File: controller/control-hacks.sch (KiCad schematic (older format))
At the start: 27 parts, among them K18 RELAY_SEPARATED, K19 RELAY_SEPARATED, K20 RELAY_SEPARATED, K21 RELAY_SEPARATED, K22 RELAY_SEPARATED, K23 RELAY_SEPARATED, K24 RELAY_SEPARATED, K25 RELAY_SEPARATED, K26 RELAY_SEPARATED

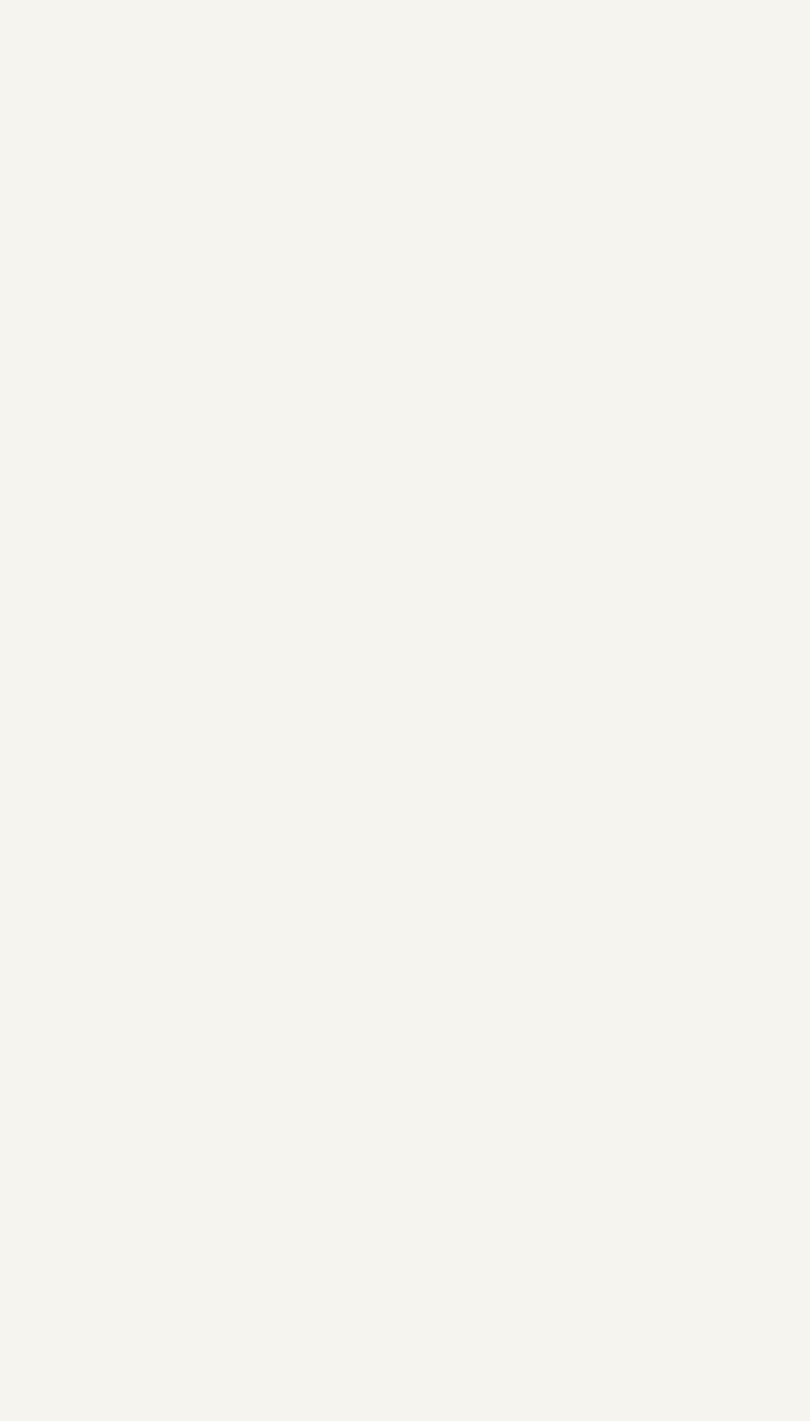
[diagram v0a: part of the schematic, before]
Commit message: Change gas pedal interface so that it supports going up and down from the middle voltage so that it's compatible with Linde forklift gas mechanism
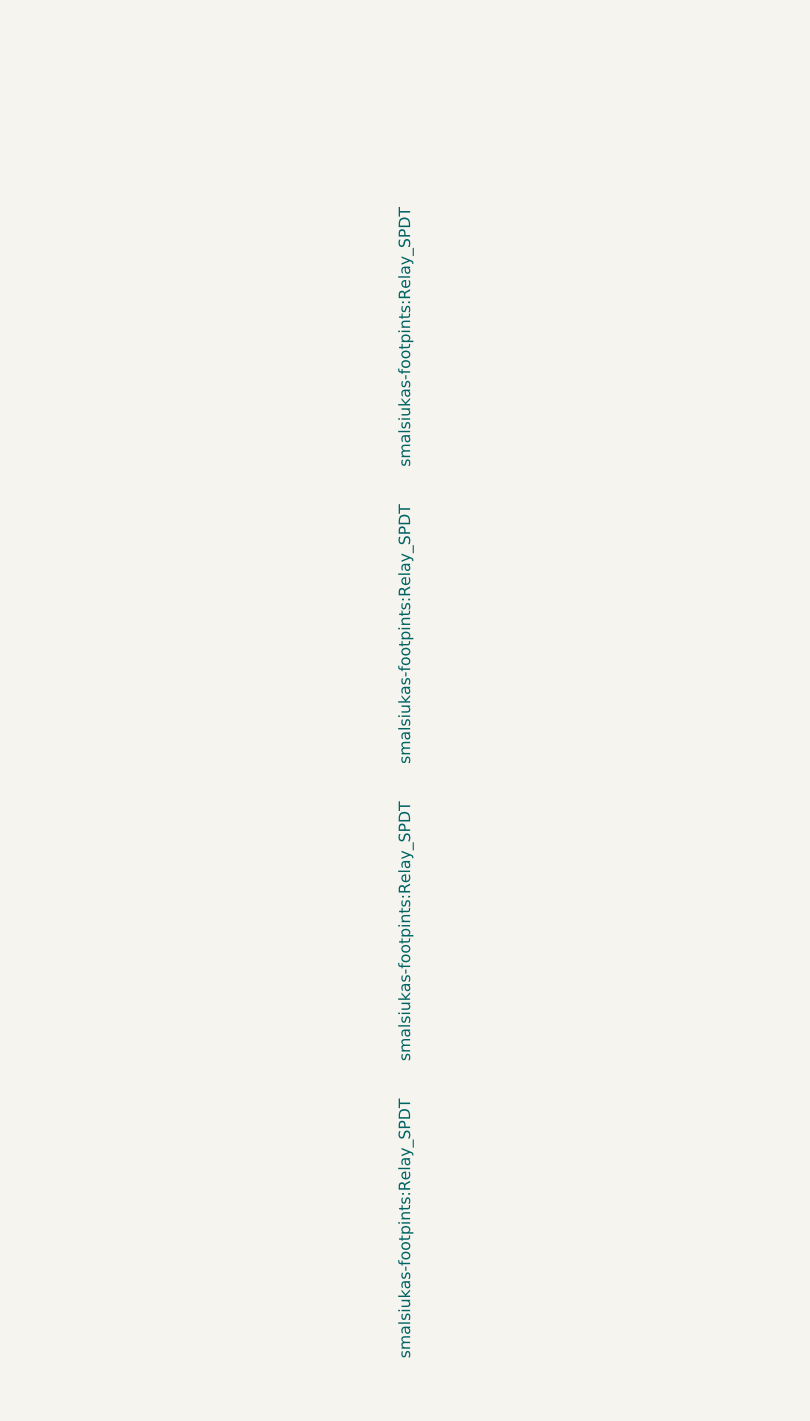
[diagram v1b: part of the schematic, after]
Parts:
- C23, C24, C25, C26, C27, C28, C29, C30, C31: footprint (none) -> Capacitors_SMD:C_0603_HandSoldering
- D18, D19, D20, D21, D22, D23, D24, D25, D26: footprint (none) -> Diodes_SMD:D_SOD-123
- K18, K19, K20, K21: footprint (none) -> smalsiukas-footpints:Relay_SPDT; Distributor (none) -> ?; Manufacturer (none) -> ?; PartNo (none) -> ?
- K18, K19, K20, K21, K22, K23, K24, K25, K26: footprint (none) -> smalsiukas-footpints:Relay_SPDT
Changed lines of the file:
@@
 F 0 "K24" V 7016 4700 50  0000 C CNN
 F 1 "RELAY_SEPARATED" V 7016 4700 50  0001 C CNN
-F 2 "" H 2150 100 50  0000 C CNN
+F 2 "smalsiukas-footpints:Relay_SPDT" H 2150 100 50  0001 C CNN
 F 3 "" H 2150 100 50  0000 C CNN
 F 4 "?" H 7250 4700 60  0001 C CNN "PartNo"
@@
 F 0 "K22" V 3100 1150 50  0000 C CNN
 F 1 "RELAY_SEPARATED" V 3066 1150 50  0001 C CNN
-F 2 "" H -1800 -3450 50  0000 C CNN
+F 2 "smalsiukas-footpints:Relay_SPDT" H -1800 -3450 50  0001 C CNN
 F 3 "" H -1800 -3450 50  0000 C CNN
 F 4 "?" H 3300 1150 60  0001 C CNN "PartNo"
@@
 F 0 "K22" V 7016 3700 50  0000 C CNN
 F 1 "RELAY_SEPARATED" V 7016 3700 50  0001 C CNN
-F 2 "" H 2150 -900 50  0000 C CNN
+F 2 "smalsiukas-footpints:Relay_SPDT" H 2150 -900 50  0001 C CNN
 F 3 "" H 2150 -900 50  0000 C CNN
 F 4 "?" H 7250 3700 60  0001 C CNN "PartNo"
@@
 F 0 "K23" V 3066 2450 50  0000 C CNN
 F 1 "RELAY_SEPARATED" V 3066 2450 50  0001 C CNN
-F 2 "" H -1800 -2150 50  0000 C CNN
+F 2 "smalsiukas-footpints:Relay_SPDT" H -1800 -2150 50  0001 C CNN
 F 3 "" H -1800 -2150 50  0000 C CNN
 F 4 "?" H 3300 2450 60  0001 C CNN "PartNo"
@@
 F 0 "K23" V 7016 4250 50  0000 C CNN
 F 1 "RELAY_SEPARATED" V 7016 4250 50  0001 C CNN
-F 2 "" H 2150 -350 50  0000 C CNN
+F 2 "smalsiukas-footpints:Relay_SPDT" H 2150 -350 50  0001 C CNN
 F 3 "" H 2150 -350 50  0000 C CNN
 F 4 "?" H 7250 4250 60  0001 C CNN "PartNo"
@@
 F 0 "K24" V 3066 3750 50  0000 C CNN
 F 1 "RELAY_SEPARATED" V 3066 3750 50  0001 C CNN
-F 2 "" H -1800 -850 50  0000 C CNN
+F 2 "smalsiukas-footpints:Relay_SPDT" H -1800 -850 50  0001 C CNN
 F 3 "" H -1800 -850 50  0000 C CNN
 F 4 "?" H 3300 3750 60  0001 C CNN "PartNo"
@@
 F 0 "K25" V 3066 5050 50  0000 C CNN
 F 1 "RELAY_SEPARATED" V 3066 5050 50  0001 C CNN
-F 2 "" H -1800 450 50  0000 C CNN
+F 2 "smalsiukas-footpints:Relay_SPDT" H -1800 450 50  0001 C CNN
 F 3 "" H -1800 450 50  0000 C CNN
 F 4 "?" H 3300 5050 60  0001 C CNN "PartNo"
@@
 F 0 "K25" V 7016 5150 50  0000 C CNN
 F 1 "RELAY_SEPARATED" V 7016 5150 50  0001 C CNN
-F 2 "" H 2150 550 50  0000 C CNN
+F 2 "smalsiukas-footpints:Relay_SPDT" H 2150 550 50  0001 C CNN
 F 3 "" H 2150 550 50  0000 C CNN
 F 4 "?" H 7250 5150 60  0001 C CNN "PartNo"
@@
 F 0 "K26" V 3066 6300 50  0000 C CNN
 F 1 "RELAY_SEPARATED" V 3066 6300 50  0001 C CNN
-F 2 "" H -1800 1700 50  0000 C CNN
+F 2 "smalsiukas-footpints:Relay_SPDT" H -1800 1700 50  0001 C CNN
 F 3 "" H -1800 1700 50  0000 C CNN
 F 4 "?" H 3300 6300 60  0001 C CNN "PartNo"
@@
 F 0 "D18" V 954 1571 50  0000 R CNN
 F 1 "D_ALT" V 1045 1571 50  0000 R CNN
-F 2 "" H -3900 -650 50  0001 C CNN
+F 2 "Diodes_SMD:D_SOD-123" H -3900 -650 50  0001 C CNN
 F 3 "" H -3900 -650 50  0001 C CNN
 	1    1000 1650
@@
 F 0 "C23" H 1115 1996 50  0000 L CNN
 F 1 "C" H 1115 1905 50  0000 L CNN
-F 2 "" H -962 0   50  0001 C CNN
+F 2 "Capacitors_SMD:C_0603_HandSoldering" H -962 0   50  0001 C CNN
 F 3 "" H -1000 150 50  0001 C CNN
 	1    1000 1950
@@
 F 0 "K18" H 1205 1196 50  0000 L CNN
 F 1 "RELAY_SEPARATED" H 1205 1105 50  0001 L CNN
-F 2 "" H -6600 -3150 50  0000 C CNN
+F 2 "smalsiukas-footpints:Relay_SPDT" H -6600 -3150 50  0000 C CNN
 F 3 "" H -6600 -3150 50  0000 C CNN
+F 4 "?" H 1050 1150 60  0001 C CNN "PartNo"
+F 5 "?" H 1050 1150 60  0001 C CNN "Manufacturer"
+F 6 "?" H 1050 1150 60  0001 C CNN "Distributor"
 	1    1050 1150
 	0    -1   -1   0
@@
 F 0 "D19" V 954 2871 50  0000 R CNN
 F 1 "D_ALT" V 1045 2871 50  0000 R CNN
-F 2 "" H -3900 650 50  0001 C CNN
+F 2 "Diodes_SMD:D_SOD-123" H -3900 650 50  0001 C CNN
 F 3 "" H -3900 650 50  0001 C CNN
 	1    1000 2950
@@
 F 0 "C24" H 1115 3296 50  0000 L CNN
 F 1 "C" H 1115 3205 50  0000 L CNN
-F 2 "" H -962 1300 50  0001 C CNN
+F 2 "Capacitors_SMD:C_0603_HandSoldering" H -962 1300 50  0001 C CNN
 F 3 "" H -1000 1450 50  0001 C CNN
 	1    1000 3250
@@
 F 0 "K18" V 7016 1550 50  0000 C CNN
 F 1 "RELAY_SEPARATED" H 7405 1505 50  0001 L CNN
-F 2 "" H -400 -2750 50  0000 C CNN
+F 2 "smalsiukas-footpints:Relay_SPDT" H -400 -2750 50  0001 C CNN
 F 3 "" H -400 -2750 50  0000 C CNN
 	2    7250 1550
@@
 F 0 "D20" V 954 4171 50  0000 R CNN
 F 1 "D_ALT" V 1045 4171 50  0000 R CNN
-F 2 "" H -3900 1950 50  0001 C CNN
+F 2 "Diodes_SMD:D_SOD-123" H -3900 1950 50  0001 C CNN
 F 3 "" H -3900 1950 50  0001 C CNN
 	1    1000 4250
@@
 F 0 "C25" H 1115 4596 50  0000 L CNN
 F 1 "C" H 1115 4505 50  0000 L CNN
-F 2 "" H -962 2600 50  0001 C CNN
+F 2 "Capacitors_SMD:C_0603_HandSoldering" H -962 2600 50  0001 C CNN
 F 3 "" H -1000 2750 50  0001 C CNN
 	1    1000 4550
@@
 F 0 "K19" H 1205 2496 50  0000 L CNN
 F 1 "RELAY_SEPARATED" H 1205 2405 50  0001 L CNN
-F 2 "" H -6600 -1850 50  0000 C CNN
+F 2 "smalsiukas-footpints:Relay_SPDT" H -6600 -1850 50  0000 C CNN
 F 3 "" H -6600 -1850 50  0000 C CNN
+F 4 "?" H 1050 2450 60  0001 C CNN "PartNo"
+F 5 "?" H 1050 2450 60  0001 C CNN "Manufacturer"
+F 6 "?" H 1050 2450 60  0001 C CNN "Distributor"
 	1    1050 2450
 	0    -1   -1   0
@@
 F 0 "D21" V 954 5471 50  0000 R CNN
 F 1 "D_ALT" V 1045 5471 50  0000 R CNN
-F 2 "" H -3900 3250 50  0001 C CNN
+F 2 "Diodes_SMD:D_SOD-123" H -3900 3250 50  0001 C CNN
 F 3 "" H -3900 3250 50  0001 C CNN
 	1    1000 5550
@@
 F 0 "C26" H 1115 5896 50  0000 L CNN
 F 1 "C" H 1115 5805 50  0000 L CNN
-F 2 "" H -962 3900 50  0001 C CNN
+F 2 "Capacitors_SMD:C_0603_HandSoldering" H -962 3900 50  0001 C CNN
 F 3 "" H -1000 4050 50  0001 C CNN
 	1    1000 5850
@@
 F 0 "K19" V 7016 2100 50  0000 C CNN
 F 1 "RELAY_SEPARATED" H 7405 2055 50  0001 L CNN
-F 2 "" H -400 -2200 50  0000 C CNN
+F 2 "smalsiukas-footpints:Relay_SPDT" H -400 -2200 50  0001 C CNN
 F 3 "" H -400 -2200 50  0000 C CNN
 	2    7250 2100
@@
 F 0 "D22" V 3204 1571 50  0000 R CNN
 F 1 "D_ALT" V 3295 1571 50  0000 R CNN
-F 2 "" H -1650 -650 50  0001 C CNN
+F 2 "Diodes_SMD:D_SOD-123" H -1650 -650 50  0001 C CNN
 F 3 "" H -1650 -650 50  0001 C CNN
 	1    3250 1650
@@
 F 0 "C27" H 3365 1996 50  0000 L CNN
 F 1 "C" H 3365 1905 50  0000 L CNN
-F 2 "" H 1288 0   50  0001 C CNN
+F 2 "Capacitors_SMD:C_0603_HandSoldering" H 1288 0   50  0001 C CNN
 F 3 "" H 1250 150 50  0001 C CNN
 	1    3250 1950
@@
 F 0 "K20" H 1205 3796 50  0000 L CNN
 F 1 "RELAY_SEPARATED" H 1205 3705 50  0001 L CNN
-F 2 "" H -6600 -550 50  0000 C CNN
+F 2 "smalsiukas-footpints:Relay_SPDT" H -6600 -550 50  0000 C CNN
 F 3 "" H -6600 -550 50  0000 C CNN
+F 4 "?" H 1050 3750 60  0001 C CNN "PartNo"
+F 5 "?" H 1050 3750 60  0001 C CNN "Manufacturer"
+F 6 "?" H 1050 3750 60  0001 C CNN "Distributor"
 	1    1050 3750
 	0    -1   -1   0
@@
 F 0 "D23" V 3204 2871 50  0000 R CNN
 F 1 "D_ALT" V 3295 2871 50  0000 R CNN
-F 2 "" H -1650 650 50  0001 C CNN
+F 2 "Diodes_SMD:D_SOD-123" H -1650 650 50  0001 C CNN
 F 3 "" H -1650 650 50  0001 C CNN
 	1    3250 2950
@@
 F 0 "C28" H 3365 3296 50  0000 L CNN
 F 1 "C" H 3365 3205 50  0000 L CNN
-F 2 "" H 1288 1300 50  0001 C CNN
+F 2 "Capacitors_SMD:C_0603_HandSoldering" H 1288 1300 50  0001 C CNN
 F 3 "" H 1250 1450 50  0001 C CNN
 	1    3250 3250
@@
 F 0 "K20" V 7016 2650 50  0000 C CNN
 F 1 "RELAY_SEPARATED" H 7405 2605 50  0001 L CNN
-F 2 "" H -400 -1650 50  0000 C CNN
+F 2 "smalsiukas-footpints:Relay_SPDT" H -400 -1650 50  0001 C CNN
 F 3 "" H -400 -1650 50  0000 C CNN
 	2    7250 2650
@@
 F 0 "D24" V 3204 4171 50  0000 R CNN
 F 1 "D_ALT" V 3295 4171 50  0000 R CNN
-F 2 "" H -1650 1950 50  0001 C CNN
+F 2 "Diodes_SMD:D_SOD-123" H -1650 1950 50  0001 C CNN
 F 3 "" H -1650 1950 50  0001 C CNN
 	1    3250 4250
@@
 F 0 "C29" H 3365 4596 50  0000 L CNN
 F 1 "C" H 3365 4505 50  0000 L CNN
-F 2 "" H 1288 2600 50  0001 C CNN
+F 2 "Capacitors_SMD:C_0603_HandSoldering" H 1288 2600 50  0001 C CNN
 F 3 "" H 1250 2750 50  0001 C CNN
 	1    3250 4550
@@
 F 0 "K21" H 1205 5096 50  0000 L CNN
 F 1 "RELAY_SEPARATED" H 1205 5005 50  0001 L CNN
-F 2 "" H -6600 750 50  0000 C CNN
+F 2 "smalsiukas-footpints:Relay_SPDT" H -6600 750 50  0000 C CNN
 F 3 "" H -6600 750 50  0000 C CNN
+F 4 "?" H 1050 5050 60  0001 C CNN "PartNo"
+F 5 "?" H 1050 5050 60  0001 C CNN "Manufacturer"
+F 6 "?" H 1050 5050 60  0001 C CNN "Distributor"
 	1    1050 5050
 	0    -1   -1   0
@@
 F 0 "D25" V 3204 5471 50  0000 R CNN
 F 1 "D_ALT" V 3295 5471 50  0000 R CNN
-F 2 "" H -1650 3250 50  0001 C CNN
+F 2 "Diodes_SMD:D_SOD-123" H -1650 3250 50  0001 C CNN
 F 3 "" H -1650 3250 50  0001 C CNN
 	1    3250 5550
@@
 F 0 "C30" H 3365 5896 50  0000 L CNN
 F 1 "C" H 3365 5805 50  0000 L CNN
-F 2 "" H 1288 3900 50  0001 C CNN
+F 2 "Capacitors_SMD:C_0603_HandSoldering" H 1288 3900 50  0001 C CNN
 F 3 "" H 1250 4050 50  0001 C CNN
 	1    3250 5850
@@
 F 0 "K21" V 7016 3150 50  0000 C CNN
 F 1 "RELAY_SEPARATED" H 7405 3105 50  0001 L CNN
-F 2 "" H -400 -1150 50  0000 C CNN
+F 2 "smalsiukas-footpints:Relay_SPDT" H -400 -1150 50  0001 C CNN
 F 3 "" H -400 -1150 50  0000 C CNN
 	2    7250 3150
@@
 F 0 "D26" V 3204 6721 50  0000 R CNN
 F 1 "D_ALT" V 3295 6721 50  0000 R CNN
-F 2 "" H -1650 4500 50  0001 C CNN
+F 2 "Diodes_SMD:D_SOD-123" H -1650 4500 50  0001 C CNN
 F 3 "" H -1650 4500 50  0001 C CNN
 	1    3250 6800
@@
 F 0 "C31" H 3365 7146 50  0000 L CNN
 F 1 "C" H 3365 7055 50  0000 L CNN
-F 2 "" H 1288 5150 50  0001 C CNN
+F 2 "Capacitors_SMD:C_0603_HandSoldering" H 1288 5150 50  0001 C CNN
 F 3 "" H 1250 5300 50  0001 C CNN
 	1    3250 7100
@@
 F 0 "K26" V 7016 5600 50  0000 C CNN
 F 1 "RELAY_SEPARATED" V 7016 5600 50  0001 C CNN
-F 2 "" H 2150 1000 50  0000 C CNN
+F 2 "smalsiukas-footpints:Relay_SPDT" H 2150 1000 50  0001 C CNN
 F 3 "" H 2150 1000 50  0000 C CNN
 F 4 "?" H 7250 5600 60  0001 C CNN "PartNo"

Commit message: More or less final controller board
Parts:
- added C43: 470u, Capacitors_ThroughHole:CP_Radial_D16.0mm_P7.50mm, symbol CP1
- added C44: C, Capacitors_SMD:C_1210_HandSoldering, symbol C
- added D58: 16V, Diodes_SMD:D_SMB_Handsoldering, symbol D_Zener
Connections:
- net VCC: now also C43.1, C44.2, D58.1 (K)
- new net GND: C43.2, C44.1, D58.2 (A)
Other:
- moved on the sheet: C23, C24, C25, C26, C27, C28, C29, C30, C31, D18, D19, D20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

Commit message: Some progress with controller board routing
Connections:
- net KEY_COLD_HACK: now also K23.4; no longer K22.4
- net KEY_HOT_HACK: now also K23.3; no longer K22.3
- net SEAT_GND_HACK: now also K22.4; no longer K23.4
- net SEAT_HACK: now also K22.3; no longer K23.3
- net VCC: now also K22.1; no longer K22.10
- net ~KEY_ENABLE_PWR: now also C28.2, D23.2 (A), K23.1; no longer C27.2, D22.2 (A), K22.1
- net ~SEAT_ENABLE_PWR: now also C27.2, D22.2 (A), K22.10; no longer C28.2, D23.2 (A), K23.1
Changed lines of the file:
@@
 Comment4 ""
 $EndDescr
-Text HLabel 7550 4350 2    60   Input ~ 0
+Text HLabel 7550 3800 2    60   Input ~ 0
 SEAT_GND_HACK
-Text HLabel 6950 4250 0    60   Input ~ 0
+Text HLabel 6950 3700 0    60   Input ~ 0
 SEAT_HACK
 Text HLabel 7550 5700 2    60   Input ~ 0
@@
 Text HLabel 7550 3250 2    60   Input ~ 0
 PARKING_HACK
-Text HLabel 6950 3700 0    60   Input ~ 0
+Text HLabel 6950 4250 0    60   Input ~ 0
 KEY_HOT_HACK
-Text HLabel 7550 3800 2    60   Input ~ 0
+Text HLabel 7550 4350 2    60   Input ~ 0
 KEY_COLD_HACK
 Text HLabel 7550 4800 2    60   Input ~ 0
@@
 F 6 "?" H 3600 1600 60  0001 C CNN "Distributor"
 	1    3600 1600
-	0    1    1    0
+	0    -1   1    0
 $EndComp
 $Comp
@@
 Wire Wire Line
 	3200 1600 3300 1600
-Text HLabel 4200 1600 2    60   Input ~ 0
+Text HLabel 4200 2900 2    60   Input ~ 0
 ~KEY_ENABLE_PWR
 Wire Wire Line
@@
 Wire Wire Line
 	3200 2900 3300 2900
-Text HLabel 4200 2900 2    60   Input ~ 0
+Text HLabel 4200 1600 2    60   Input ~ 0
 ~SEAT_ENABLE_PWR
 Wire Wire Line
@@
 $EndComp
 $Comp
-L GND #PWR022
+L GND #PWR024
 U 1 1 58C9BB32
 P 3750 1100
-F 0 "#PWR022" H -600 -2450 50  0001 C CNN
+F 0 "#PWR024" H -600 -2450 50  0001 C CNN
 F 1 "GND" H 3755 927 50  0000 C CNN
 F 2 "" H -600 -2200 50  0001 C CNN
@@
 $EndComp
 $Comp
-L GND #PWR023
+L GND #PWR025
 U 1 1 58C9BB3F
 P 4500 1100
-F 0 "#PWR023" H 150 -2450 50  0001 C CNN
+F 0 "#PWR025" H 150 -2450 50  0001 C CNN
 F 1 "GND" H 4505 927 50  0000 C CNN
 F 2 "" H 150 -2200 50  0001 C CNN

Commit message: Finish the routing, add some significant fixes: *correct to-252 pin numbering * longer pads for relays * fix footprint of the optocouplers
Also finish the routing
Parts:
- C44: value C -> 1u; Distributor ? -> 2320928
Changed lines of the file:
@@
 $EndComp
 $Comp
-L GND #PWR024
+L GND #PWR033
 U 1 1 58C9BB32
 P 3750 1100
-F 0 "#PWR024" H -600 -2450 50  0001 C CNN
+F 0 "#PWR033" H -600 -2450 50  0001 C CNN
 F 1 "GND" H 3755 927 50  0000 C CNN
 F 2 "" H -600 -2200 50  0001 C CNN
@@
 P 4100 950
 F 0 "C44" H 3985 904 50  0000 R CNN
-F 1 "C" H 3985 995 50  0000 R CNN
+F 1 "1u" H 3985 995 50  0000 R CNN
 F 2 "Capacitors_SMD:C_1210_HandSoldering" H -4012 -4900 50  0001 C CNN
 F 3 "" H -4050 -4750 50  0001 C CNN
 F 4 "?" H 4100 950 60  0001 C CNN "PartNo"
 F 5 "?" H 4100 950 60  0001 C CNN "Manufacturer"
-F 6 "?" H 4100 950 60  0001 C CNN "Distributor"
+F 6 "2320928" H 4100 950 60  0001 C CNN "Distributor"
 	1    4100 950
 	-1   0    0    1
 $EndComp
 $Comp
-L GND #PWR025
+L GND #PWR034
 U 1 1 58C9BB3F
 P 4500 1100
-F 0 "#PWR025" H 150 -2450 50  0001 C CNN
+F 0 "#PWR034" H 150 -2450 50  0001 C CNN
 F 1 "GND" H 4505 927 50  0000 C CNN
 F 2 "" H 150 -2200 50  0001 C CNN
